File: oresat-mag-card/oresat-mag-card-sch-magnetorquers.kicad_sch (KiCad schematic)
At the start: 67 parts, among them U12 STSPIN250, U13 STSPIN250, U14 INA185A2, U15 INA185A2, U16 STSPIN250, U17 INA185A2

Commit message: Mag Card v1.1
Swapped out MT connectors which were unbearably small, fixed 3D models, fixed IMU address, added versioning. Brought OPD up to latest standards.
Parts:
- R58, R60: DPN RMCF0603FT237RCT-ND -> RMCF0603FT23K7CT-ND; MPN RMCF0603FT237R -> RMCF0603FT23K7
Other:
- note added: "X/Y "Rod" Magnetorquer 30 AWG with Kapton insulation Number of wire turns: 1700 +/- 2% Total resistance: 151 ohm +/- 10%"
- note added: "Z "Ring" Magnetorquer 30 AWG with Kapton insulation Number of wire turns: 500 +/- 1% Total resistance: 60 ohm +/- 10%"
- note removed: "Magnetorquer Spec: 1.3 Ω 0.6 A max each"
- moved on the sheet: C59, C60, C61, C62, C63, C64, C67, C69, R71, R72, R73, R74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

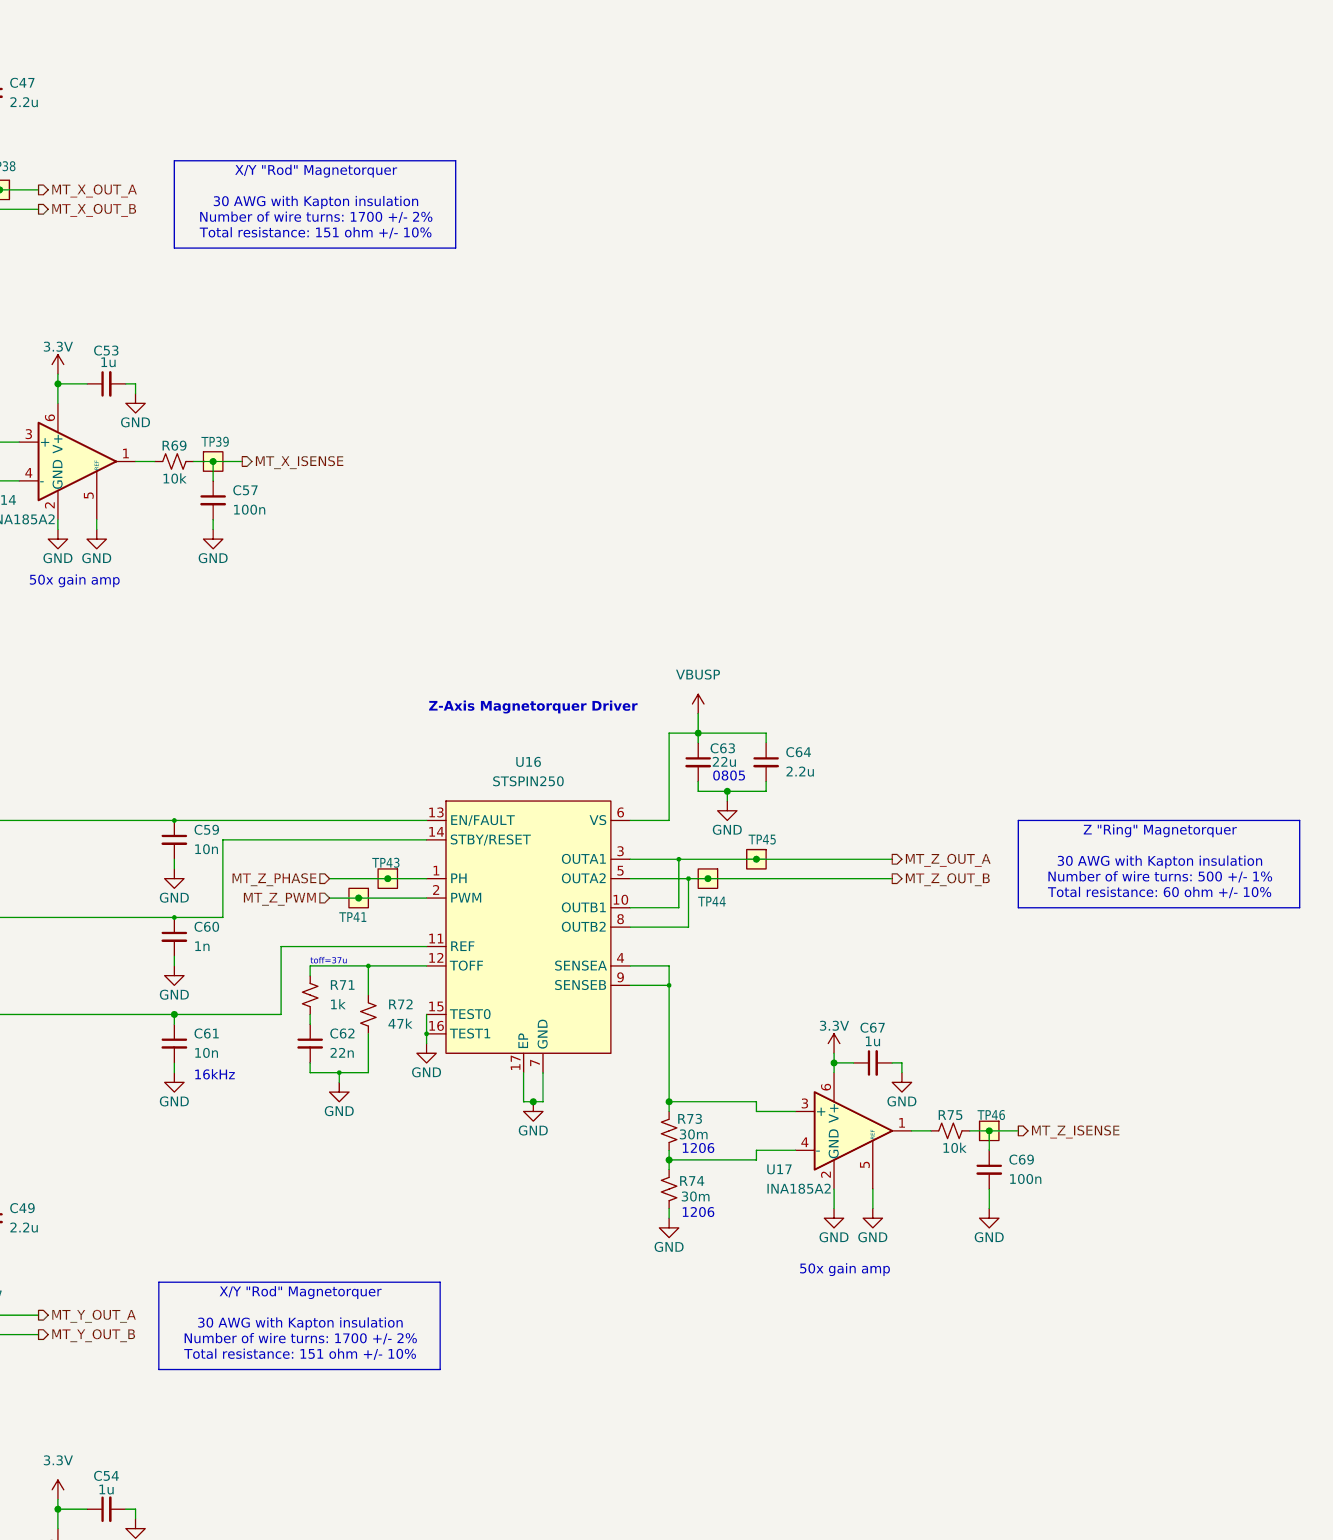
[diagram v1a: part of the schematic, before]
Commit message: Added GND test points, extended a cutout around the IMU for less PCB stress/strain near the IMU, added MT details to the schematic.
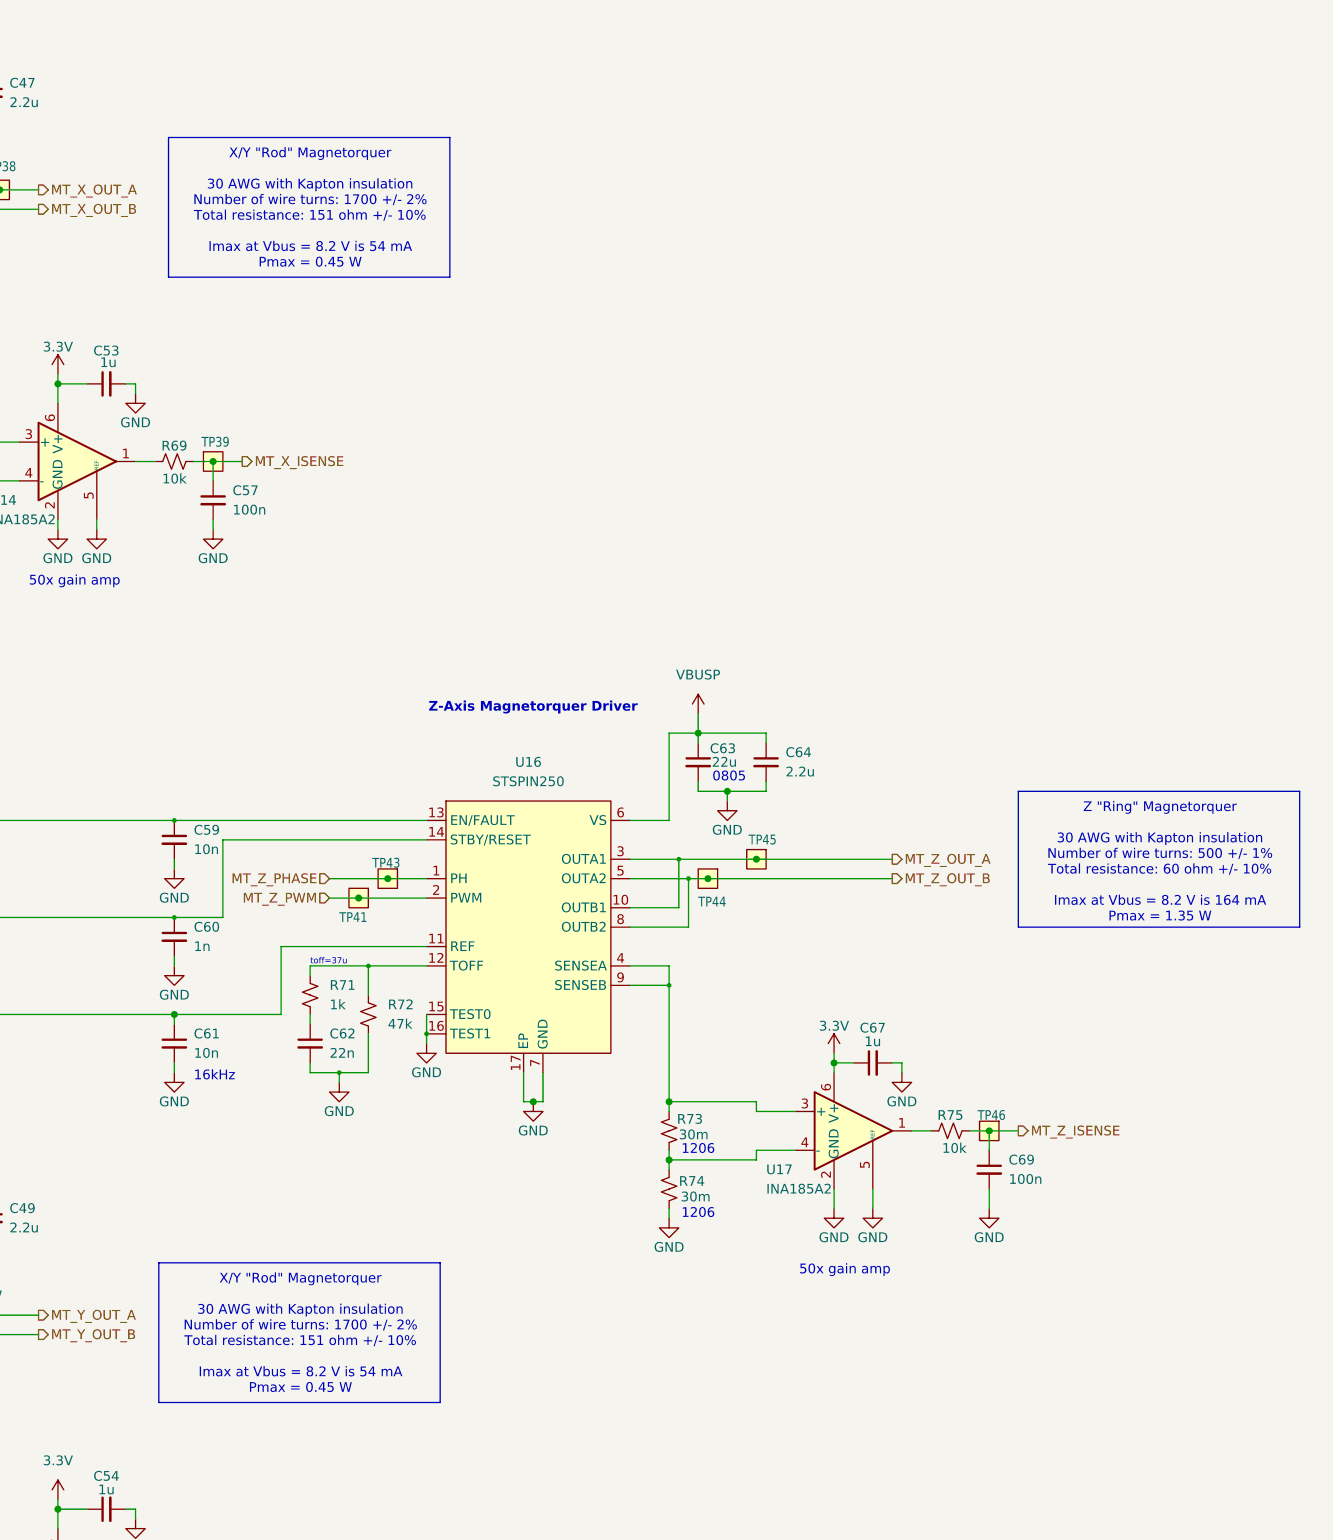
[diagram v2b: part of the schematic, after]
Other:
- note added: "X/Y "Rod" Magnetorquer 30 AWG with Kapton insulation Number of wire turns: 1700 +/- 2% Total resistance: 151 ohm +/- 10% Imax at Vbus = 8.2 V is 54 mA Pmax = 0.45 W"
- note added: "Z "Ring" Magnetorquer 30 AWG with Kapton insulation Number of wire turns: 500 +/- 1% Total resistance: 60 ohm +/- 10% Imax at Vbus = 8.2 V is 164 mA Pmax = 1.35 W"
- note removed: "X/Y "Rod" Magnetorquer 30 AWG with Kapton insulation Number of wire turns: 1700 +/- 2% Total resistance: 151 ohm +/- 10%"
- note removed: "Z "Ring" Magnetorquer 30 AWG with Kapton insulation Number of wire turns: 500 +/- 1% Total resistance: 60 ohm +/- 10%"
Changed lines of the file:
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@@
 	)
 	(rectangle
-		(start 215.9 44.45)
-		(end 252.73 55.88)
+		(start 215.138 41.402)
+		(end 251.968 59.69)
 		(stroke
 			(width 0)
@@
 	)
 	(rectangle
-		(start 213.868 191.262)
-		(end 250.698 202.692)
+		(start 213.868 188.722)
+		(end 250.698 207.01)
 		(stroke
 			(width 0)
@@
 	)
 	(rectangle
-		(start 326.39 130.81)
-		(end 363.22 142.24)
+		(start 326.39 127)
+		(end 363.22 144.78)
 		(stroke
 			(width 0)
@@
 		)
 	)
-	(text "X/Y \"Rod\" Magnetorquer\n\n30 AWG with Kapton insulation\nNumber of wire turns: 1700 +/- 2%\nTotal resistance: 151 ohm +/- 10%\n"
-		(exclude_from_sim no)
-		(at 232.41 196.85 0)
+	(text "X/Y \"Rod\" Magnetorquer\n\n30 AWG with Kapton insulation\nNumber of wire turns: 1700 +/- 2%\nTotal resistance: 151 ohm +/- 10%\n\nImax at Vbus = 8.2 V is 54 mA\nPmax = 0.45 W\n"
+		(exclude_from_sim no)
+		(at 232.41 198.12 0)
 		(effects
 			(font
@@
 		)
 	)
-	(text "Z \"Ring\" Magnetorquer\n\n30 AWG with Kapton insulation\nNumber of wire turns: 500 +/- 1%\nTotal resistance: 60 ohm +/- 10%\n"
+	(text "Z \"Ring\" Magnetorquer\n\n30 AWG with Kapton insulation\nNumber of wire turns: 500 +/- 1%\nTotal resistance: 60 ohm +/- 10%\n\nImax at Vbus = 8.2 V is 164 mA\nPmax = 1.35 W"
 		(exclude_from_sim no)
 		(at 344.932 136.398 0)
@@
 		)
 	)
+	(text "X/Y \"Rod\" Magnetorquer\n\n30 AWG with Kapton insulation\nNumber of wire turns: 1700 +/- 2%\nTotal resistance: 151 ohm +/- 10%\n\nImax at Vbus = 8.2 V is 54 mA\nPmax = 0.45 W\n"
+		(exclude_from_sim no)
+		(at 233.68 50.8 0)
+		(effects
+			(font
+				(size 1.27 1.27)
+			)
+		)
+	)
 	(text "50x gain amp"
 		(exclude_from_sim no)
@@
 		)
 	)
-	(text "X/Y \"Rod\" Magnetorquer\n\n30 AWG with Kapton insulation\nNumber of wire turns: 1700 +/- 2%\nTotal resistance: 151 ohm +/- 10%\n"
-		(exclude_from_sim no)
-		(at 234.442 50.038 0)
-		(effects
-			(font
-				(size 1.27 1.27)
-			)
-		)
-	)
